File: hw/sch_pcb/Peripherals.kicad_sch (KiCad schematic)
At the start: 49 parts

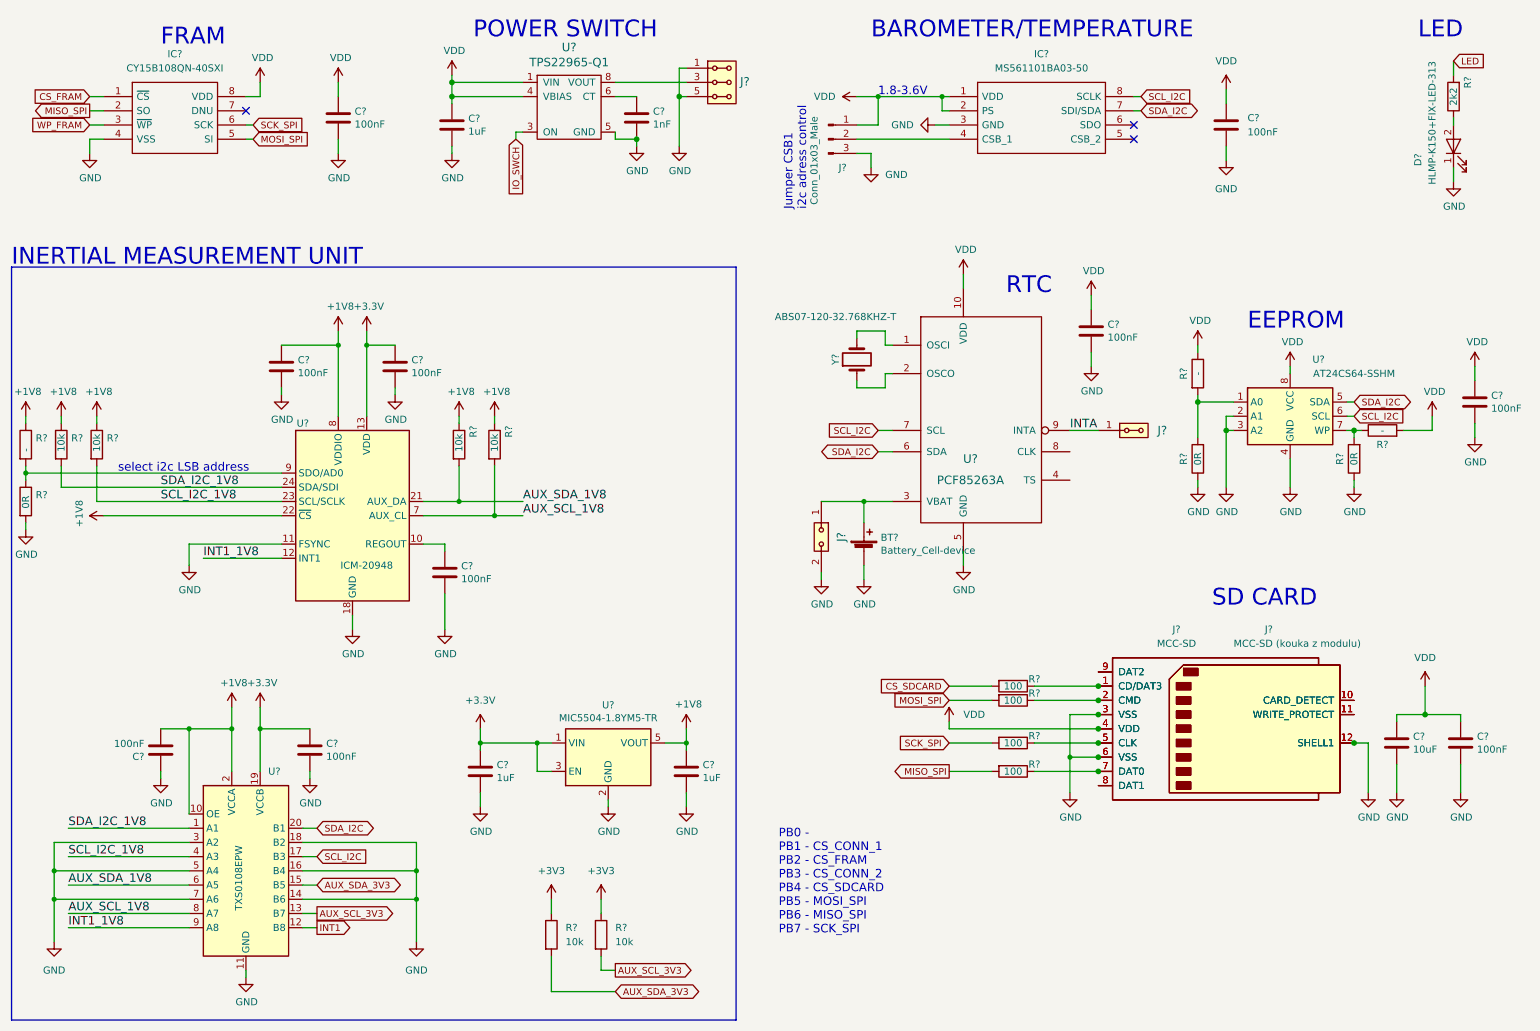
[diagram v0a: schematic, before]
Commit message: schematics update - LTC4041, TPS631000
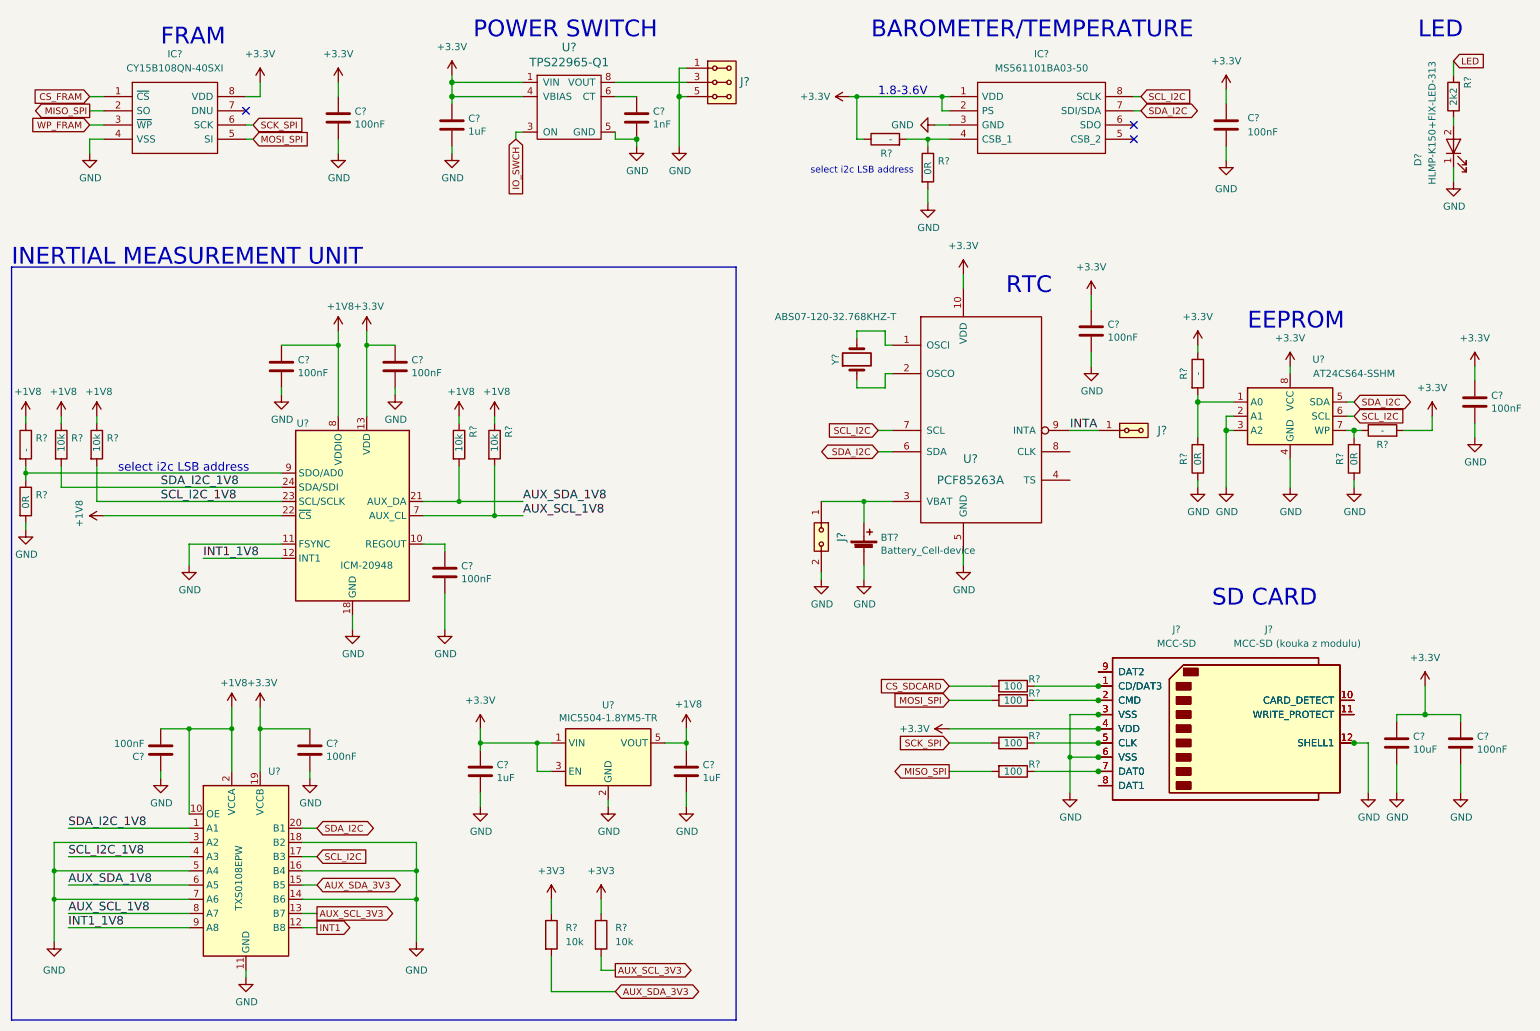
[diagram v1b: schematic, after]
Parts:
- removed J?: Conn_01x03_Male, symbol Connector:Conn_01x03_Male
- added R?: -, Mlab_R:SMD-0603, symbol Device:R
- added R?: 0R, Mlab_R:SMD-0603, symbol Device:R
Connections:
- net VDD is gone; now on net +3.3V: C?.1, C?.1, C?.1, C?.1, C?.1, C?.1, C?.1, IC?.1 (VDD), IC?.2 (PS), IC?.8 (VDD), J?.4 (VDD), J?.4 (VDD), R?.1, R?.2, U?.1 (VIN), U?.10 (VDD), U?.2 (VIN), U?.4 (VBIAS), U?.8 (VCC)
- net +3.3V: now also R?.1
- net GND: now also R?.2
- net at IC?.4 (CSB_1): now also R?.1, R?.2
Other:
- note removed: "Jumper CSB1 i2c adress control"
- note removed: "PB0 - PB1 - CS_CONN_1 PB2 - CS_FRAM PB3 - CS_CONN_2 PB4 - CS_SDCARD PB5 - MOSI_SPI PB6 - MISO_SPI PB7 - SCK_SPI"
